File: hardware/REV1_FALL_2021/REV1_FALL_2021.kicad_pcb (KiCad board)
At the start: 2 copper layers, 5 parts, among them U1 Teensy3.6_All_Pins, U2 PA16165_Breakout, U3 MPL3115A2_Breakout, U4 BNO055_Breakout, U5 RFM69HCW_Breakout

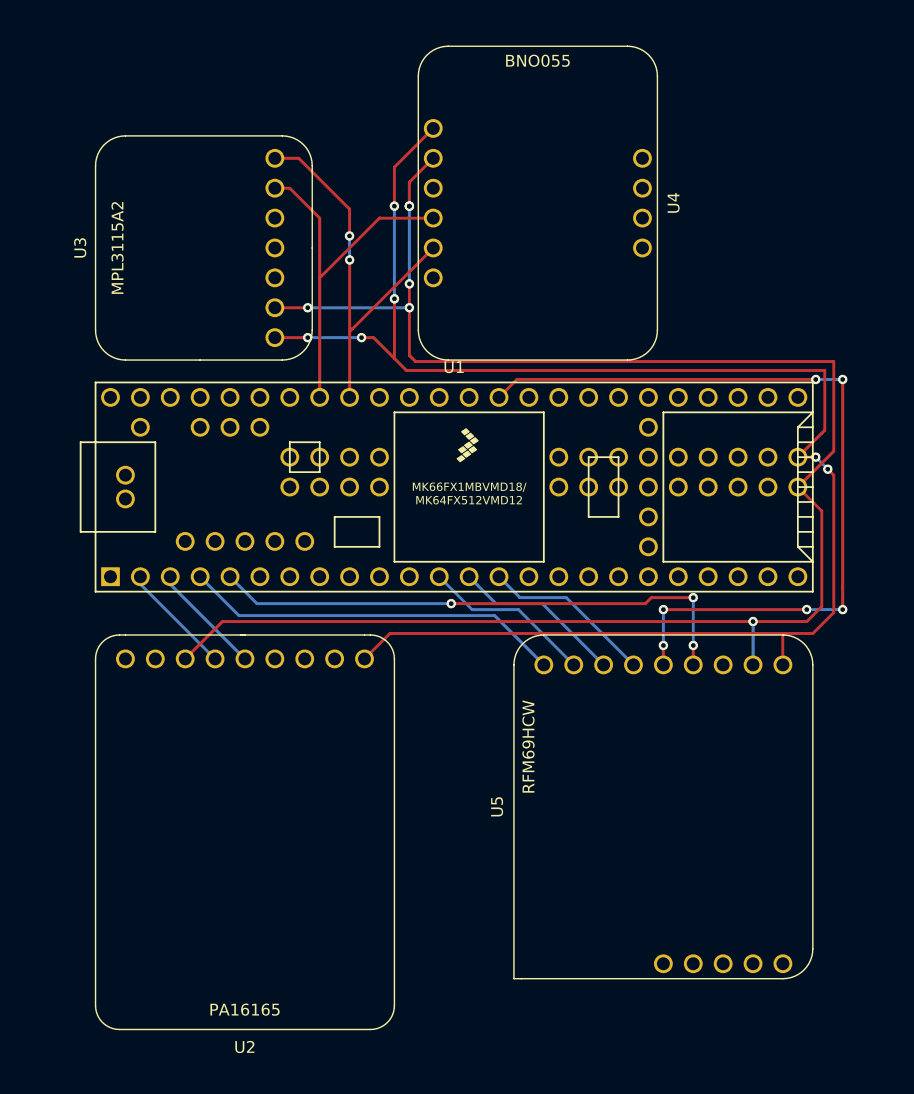
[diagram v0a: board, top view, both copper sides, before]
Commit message: Verify pin connections on layout and fix mistakes
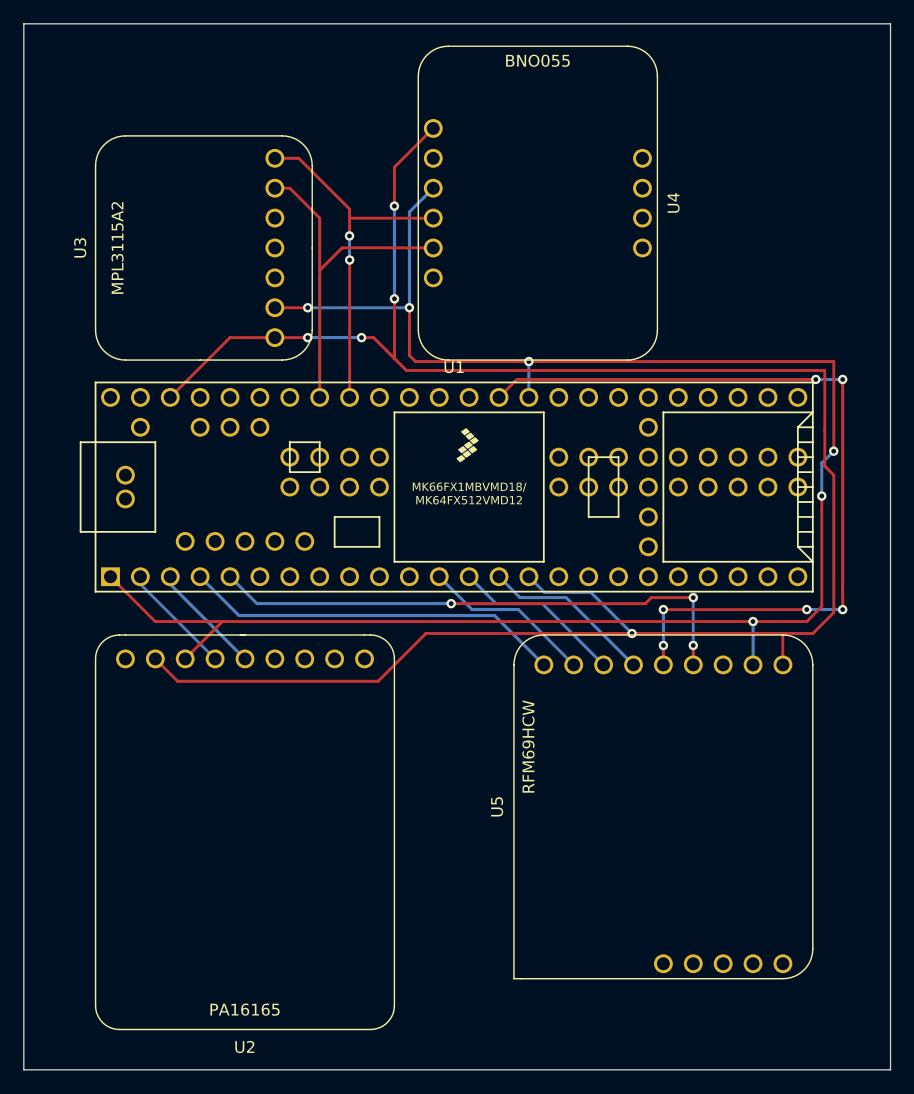
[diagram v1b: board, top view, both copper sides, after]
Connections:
- U1 pad 1: Net-(U1-Pad1) -> /GND
- U1 pad 10: Net-(U1-Pad10) -> (no net)
- U1 pad 11: Net-(U1-Pad11) -> (no net)
- U1 pad 15: Net-(U1-Pad15) -> /3.3V
- U1 pad 16: Net-(U1-Pad16) -> (no net)
- U1 pad 17: Net-(U1-Pad17) -> (no net)
- U1 pad 18: Net-(U1-Pad18) -> (no net)
- U1 pad 19: Net-(U1-Pad19) -> (no net)
- U1 pad 20: Net-(U1-Pad20) -> (no net)
- U1 pad 21: Net-(U1-Pad21) -> (no net)
- U1 pad 22: Net-(U1-Pad22) -> (no net)
- U1 pad 23: Net-(U1-Pad23) -> (no net)
- U1 pad 24: Net-(U1-Pad24) -> (no net)
- U1 pad 25: Net-(U1-Pad25) -> (no net)
- U1 pad 26: Net-(U1-Pad26) -> (no net)
- U1 pad 27: Net-(U1-Pad27) -> (no net)
- U1 pad 28: Net-(U1-Pad28) -> (no net)
- U1 pad 29: Net-(U1-Pad29) -> (no net)
- U1 pad 30: Net-(U1-Pad30) -> (no net)
- U1 pad 31: Net-(U1-Pad31) -> (no net)
- U1 pad 32: Net-(U1-Pad32) -> (no net)
- U1 pad 33: Net-(U1-Pad33) -> (no net)
- U1 pad 34: Net-(U1-Pad34) -> (no net)
- U1 pad 35: Net-(U1-Pad35) -> (no net)
- U1 pad 36: Net-(U1-Pad36) -> (no net)
- U1 pad 37: Net-(U1-Pad37) -> (no net)
- U1 pad 38: Net-(U1-Pad38) -> (no net)
- U1 pad 39: Net-(U1-Pad39) -> /GND
- U1 pad 41: Net-(U1-Pad41) -> (no net)
- U1 pad 42: Net-(U1-Pad42) -> (no net)
- U1 pad 43: Net-(U1-Pad43) -> (no net)
- U1 pad 44: Net-(U1-Pad44) -> (no net)
- U1 pad 47: Net-(U1-Pad47) -> (no net)
- U1 pad 48: Net-(U1-Pad48) -> (no net)
- U1 pad 49: Net-(U1-Pad49) -> (no net)
- U1 pad 50: Net-(U1-Pad50) -> (no net)
- U1 pad 51: Net-(U1-Pad51) -> /3.3V
- U1 pad 52: Net-(U1-Pad52) -> (no net)
- U1 pad 53: Net-(U1-Pad53) -> (no net)
- U1 pad 54: Net-(U1-Pad54) -> (no net)
- U1 pad 55: Net-(U1-Pad55) -> (no net)
- U1 pad 56: Net-(U1-Pad56) -> (no net)
- U1 pad 57: Net-(U1-Pad57) -> (no net)
- U1 pad 58: Net-(U1-Pad58) -> (no net)
- U1 pad 59: Net-(U1-Pad59) -> (no net)
- U1 pad 6: Net-(U1-Pad6) -> (no net)
- U1 pad 60: Net-(U1-Pad60) -> (no net)
- U1 pad 61: Net-(U1-Pad61) -> (no net)
- U1 pad 62: Net-(U1-Pad62) -> (no net)
- U1 pad 63: Net-(U1-Pad63) -> (no net)
- U1 pad 64: Net-(U1-Pad64) -> (no net)
- U1 pad 65: Net-(U1-Pad65) -> (no net)
- U1 pad 66: Net-(U1-Pad66) -> (no net)
- U1 pad 67: Net-(U1-Pad67) -> (no net)
- U1 pad 68: Net-(U1-Pad68) -> (no net)
- U1 pad 69: Net-(U1-Pad69) -> (no net)
- U1 pad 7: Net-(U1-Pad7) -> (no net)
- U1 pad 70: Net-(U1-Pad70) -> (no net)
- U1 pad 71: Net-(U1-Pad71) -> (no net)
- U1 pad 72: Net-(U1-Pad72) -> (no net)
- U1 pad 73: Net-(U1-Pad73) -> (no net)
- U1 pad 74: /GND -> (no net)
- U1 pad 75: /3.3V -> (no net)
- U1 pad 76: Net-(U1-Pad76) -> (no net)
- U1 pad 77: Net-(U1-Pad77) -> (no net)
- U1 pad 78: Net-(U1-Pad78) -> (no net)
- U1 pad 79: Net-(U1-Pad79) -> (no net)
- U1 pad 8: Net-(U1-Pad8) -> (no net)
- U1 pad 80: Net-(U1-Pad80) -> (no net)
- U1 pad 81: Net-(U1-Pad81) -> (no net)
- U1 pad 82: Net-(U1-Pad82) -> (no net)
- U1 pad 83: Net-(U1-Pad83) -> (no net)
- U1 pad 84: Net-(U1-Pad84) -> (no net)
- U1 pad 85: Net-(U1-Pad85) -> (no net)
- U1 pad 86: Net-(U1-Pad86) -> (no net)
- U1 pad 87: Net-(U1-Pad87) -> (no net)
- U1 pad 88: Net-(U1-Pad88) -> (no net)
- U1 pad 9: Net-(U1-Pad9) -> (no net)
- U2 pad 1: /3.3V -> (no net)
- U2 pad 2: Net-(U2-Pad2) -> (no net)
- U2 pad 3: Net-(U2-Pad3) -> (no net)
- U2 pad 4: Net-(U2-Pad4) -> (no net)
- U2 pad 8: Net-(U2-Pad8) -> /3.3V
- U2 pad 9: Net-(U2-Pad9) -> (no net)
- U3 pad 3: Net-(U3-Pad3) -> (no net)
- U3 pad 4: Net-(U3-Pad4) -> (no net)
- U3 pad 5: Net-(U3-Pad5) -> (no net)
- U4 pad 10: Net-(U4-Pad10) -> (no net)
- U4 pad 2: /GND -> (no net)
- U4 pad 3: Net-(U4-Pad3) -> /GND
- U4 pad 4: /SCL0 -> /SDA0
- U4 pad 5: /SDA0 -> /SCL0
- U4 pad 6: Net-(U4-Pad6) -> (no net)
- U4 pad 7: Net-(U4-Pad7) -> (no net)
- U4 pad 8: Net-(U4-Pad8) -> (no net)
- U4 pad 9: Net-(U4-Pad9) -> (no net)
- U5 pad 10: Net-(U5-Pad10) -> (no net)
- U5 pad 11: Net-(U5-Pad11) -> (no net)
- U5 pad 12: Net-(U5-Pad12) -> (no net)
- U5 pad 13: Net-(U5-Pad13) -> (no net)
- U5 pad 14: Net-(U5-Pad14) -> (no net)
- U5 pad 3: Net-(U5-Pad3) -> (no net)
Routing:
- net /3.3V: track 137.1 -> 175.4 mm, vias 6 -> 5
- net /GND: track 147.9 -> 157.8 mm
- net /SDA0: track 34.2 -> 31.3 mm
- net /SCL0: track 31.9 -> 30.5 mm
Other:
- board outline added: 73.7 x 88.9 mm

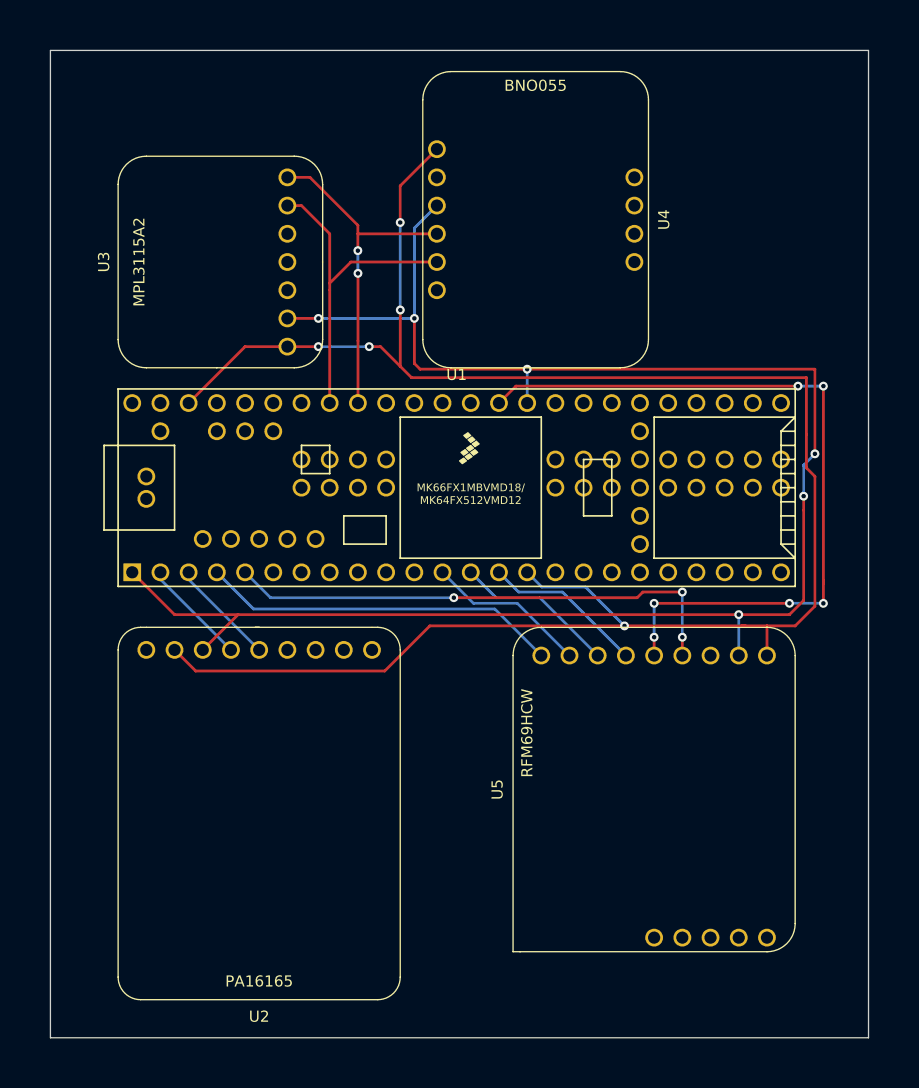
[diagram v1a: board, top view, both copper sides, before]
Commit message: add GND filled zones
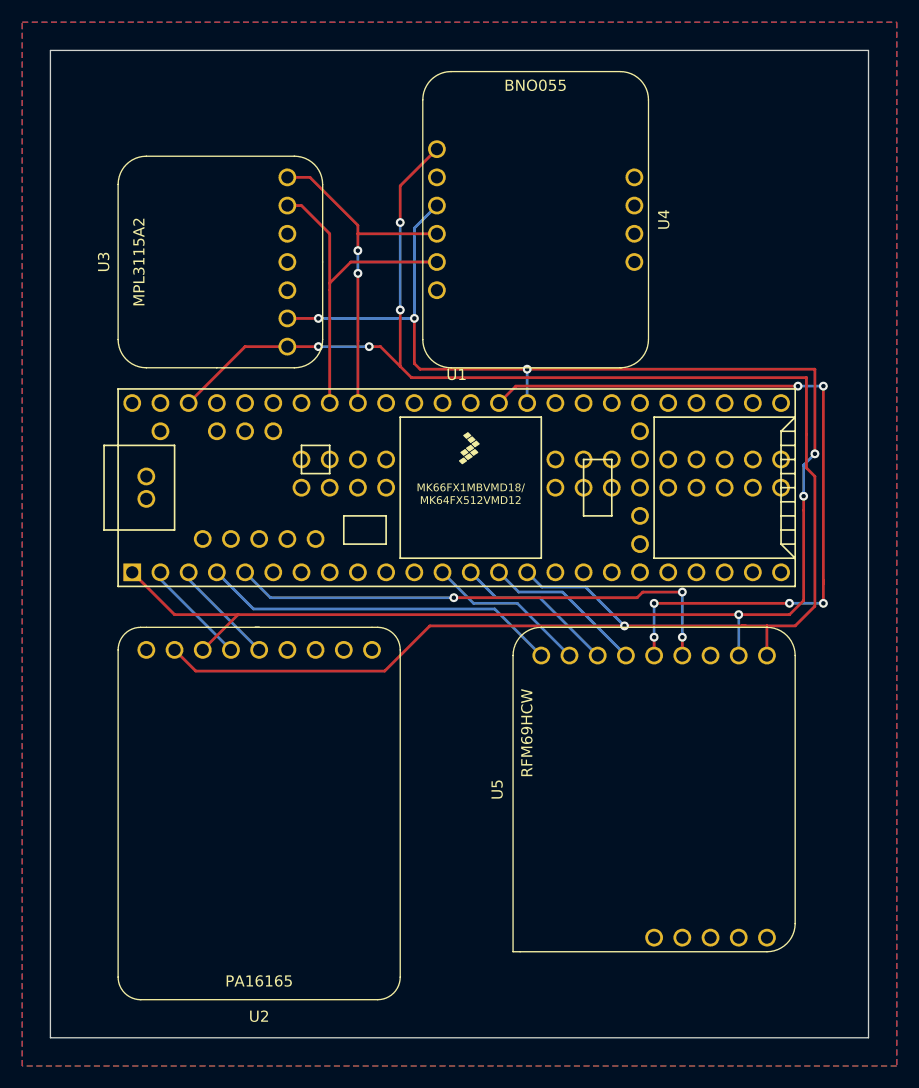
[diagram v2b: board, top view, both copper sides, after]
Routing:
- added copper zone on B.Cu, net /GND
- added copper zone on F.Cu, net /GND
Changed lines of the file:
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@@
     (user_trace_width 0.508)
     (trace_clearance 0.2)
-    (zone_clearance 0.508)
+    (zone_clearance 0.25)
     (zone_45_only no)
     (trace_min 0.2)
@@
   (segment (start 129.470998 91.497998) (end 125.533998 91.497998) (width 0.25) (layer B.Cu) (net 12))
   (segment (start 129.470998 91.497998) (end 132.969 94.996) (width 0.25) (layer B.Cu) (net 12))
+  (zone (net 11) (net_name /GND) (layer F.Cu) (hatch edge 0.508)
+    (connect_pads (clearance 0.25))
+    (min_thickness 0.24)
+    (fill yes (arc_segments 32) (thermal_gap 0.508) (thermal_bridge_width 0.508))
+    (polygon
+      (pts
+        (xy 157.48 134.62) (xy 78.74 134.62) (xy 78.74 40.64) (xy 157.48 40.64)
+      )
+    )
+  )
+  (zone (net 11) (net_name /GND) (layer B.Cu) (hatch edge 0.508)
+    (connect_pads (clearance 0.25))
+    (min_thickness 0.24)
+    (fill yes (arc_segments 32) (thermal_gap 0.508) (thermal_bridge_width 0.508))
+    (polygon
+      (pts
+        (xy 157.48 134.62) (xy 78.74 134.62) (xy 78.74 40.64) (xy 157.48 40.64)
+      )
+    )
+  )
 )

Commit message: start schematic
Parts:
- added BT101: Battery_Cell, Olin_Rocketry:MyBatteryHolder_MPD_BH-18650-PC2, F.Cu at (64.8, 82.5)
- added BT102: Battery_Cell, Olin_Rocketry:MyBatteryHolder_MPD_BH-18650-PC2, F.Cu at (64.8, 61.0)
- added C201: C_0.1uF, Capacitor_SMD:C_0805_2012Metric_Pad1.18x1.45mm_HandSolder, F.Cu at (73.0, 167.0)
- added C202: C_0.1uF, Capacitor_SMD:C_0805_2012Metric_Pad1.18x1.45mm_HandSolder, F.Cu at (67.9, 167.0)
- added C203: C, Capacitor_SMD:C_0805_2012Metric_Pad1.18x1.45mm_HandSolder, F.Cu at (76.8, 182.2)
- added C301: C_0.1uF, Capacitor_SMD:C_0805_2012Metric_Pad1.18x1.45mm_HandSolder, F.Cu at (115.2, 10.6)
- added C302: C_0.1uF, Capacitor_SMD:C_0805_2012Metric_Pad1.18x1.45mm_HandSolder, F.Cu at (115.2, 15.4)
- added C303: C, Capacitor_SMD:C_0805_2012Metric_Pad1.18x1.45mm_HandSolder, F.Cu at (110.2, 9.90)
- added J101: Screw_Terminal_01x02, TerminalBlock:TerminalBlock_bornier-2_P5.08mm, F.Cu at (127.6, 168.3)
- added Q101: Q_NMOS_GDS, footprints:TO-220-3, F.Cu at (112.4, 170.8)
- added R101: R_15k, Resistor_SMD:R_0805_2012Metric_Pad1.20x1.40mm_HandSolder, F.Cu at (79.4, 167.0)
- added R102: R_5k, Resistor_SMD:R_0805_2012Metric_Pad1.20x1.40mm_HandSolder, F.Cu at (65.0, -11.4)
- added R103: R_10k, Resistor_SMD:R_0805_2012Metric_Pad1.20x1.40mm_HandSolder, F.Cu at (106.0, 170.8)
- added R201: R_250, Resistor_SMD:R_0805_2012Metric_Pad1.20x1.40mm_HandSolder, F.Cu at (62.9, 167.0)
- added R202: R_10k, Resistor_SMD:R_0805_2012Metric_Pad1.20x1.40mm_HandSolder, F.Cu at (83.2, 182.2)
- added R301: R_250, Resistor_SMD:R_0805_2012Metric_Pad1.20x1.40mm_HandSolder, F.Cu at (79.7, -10.1)
- added R302: R_10k, Resistor_SMD:R_0805_2012Metric_Pad1.20x1.40mm_HandSolder, F.Cu at (113.2, 5.81)
- added U201: TPS2113ADRBR, footprints:TPS2113ADRBR, F.Cu at (104.8, 167.0)
- added U301: TPS2113ADRBR, footprints:TPS2113ADRBR, F.Cu at (89.5, 167.0)
- moved U3 90.0 mm to (74.3, 149.5), turned to 180 degrees
- moved U4 82.8 mm to (70.5, 120.8), turned to 0 degrees
- moved U1 50.9 mm to (94.6, 127.9), turned to 90 degrees
- moved U2 41.4 mm to (123.8, 145.7), turned to 270 degrees
- moved U5 13.8 mm to (121.8, 110.1), turned to 180 degrees
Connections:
- net /GND renamed GND
- U1 pad 32: (no net) -> /TPS_1_STAT
- U1 pad 33: (no net) -> /TPS_2_STAT
- U1 pad 34: (no net) -> /BALANCE_CONTROL
- U1 pad 36: (no net) -> /E-MATCH_TRIGGER
- U1 pad 53: (no net) -> /V_TEENSY
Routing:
- removed copper zone on B.Cu, net GND
- removed copper zone on F.Cu, net GND
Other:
- board outline removed
